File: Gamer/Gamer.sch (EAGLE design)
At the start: 44 parts, among them J1 HEADER-1X8, J2 HEADER-1X8, J3 HEADER-1X8, J4 HEADER-1X8, J5 HEADER-1X8, J6 HEADER-1X8, J7 HEADER-1X8, J8 HEADER-1X8, U1 MMA8653FCR1, U2 ATTINY48, U3 ULN2803AFWG, U4 ATTINY48, U5 ULN2803AFWG, U6 ATTINY48, U7 ULN2803AFWG, U8 ATTINY48, U9 ULN2803AFWG

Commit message: gamer - partial routing, with ground plane and vias, and some hand routing
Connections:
- net 3.3V_2 renamed 3V3_2
- removed net 3.3V_1: P1.1
- removed net GND: A.1, B.1, C1.2, C2.2, C3.2, C4.2, C5.2, C6.2, C7.2, C8.2, DOWN.4, LEFT.4, P1.9, PROG1.6, PROG2.6, PROG3.6, PROG4.6, RIGHT.4, SELECT.4, START.4, U1.AAGND, U1.AGND, U1.GND, U2.AGND, U2.GND, U3.GND, U4.AGND, U4.GND, U5.GND, U6.AGND, U6.GND, U7.GND, U8.AGND, U8.GND, U9.GND, UP.4
- removed net SCL: R1.1, U1.SCL
- removed net SDA: R2.1, U1.SDA
- removed net VCC: C1.1, C2.1, C4.1, C5.1, C6.1, C7.1, C8.1, PROG1.2, PROG2.2, PROG3.2, PROG4.2, R1.2, R2.2, R3.1, R4.1, R5.1, R6.1, U1.VDD, U1.VDDIO, U2.AVCC, U2.VCC, U3.COMMON, U4.AVCC, U4.VCC, U5.COMMON, U6.AVCC, U6.VCC, U7.COMMON, U8.AVCC, U8.VCC, U9.COMMON
- new net 3V3: C1.1, C2.1, C4.1, C5.1, C6.1, C7.1, C8.1, P1.1, PROG1.2, PROG2.2, PROG3.2, PROG4.2, R1.2, R2.2, R3.1, R4.1, R5.1, R6.1, U1.VDD, U1.VDDIO, U2.AVCC, U2.VCC, U3.COMMON, U4.AVCC, U4.VCC, U5.COMMON, U6.AVCC, U6.VCC, U7.COMMON, U8.AVCC, U8.VCC, U9.COMMON
- new net EEE: A.1, B.1, C1.2, C2.2, C3.2, C4.2, C5.2, C6.2, C7.2, C8.2, DOWN.4, LEFT.4, P1.9, PROG1.6, PROG2.6, PROG3.6, PROG4.6, RIGHT.4, SELECT.3, START.3, U1.AAGND, U1.AGND, U1.GND, U2.AGND, U2.GND, U3.GND, U4.AGND, U4.GND, U5.GND, U6.AGND, U6.GND, U7.GND, U8.AGND, U8.GND, U9.GND, UP.4
- new net N$1: START.4
- net 2/SDA: now also R2.1, U1.SDA
- net 3/SCL: now also R1.1, U1.SCL
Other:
- moved on the sheet: R2
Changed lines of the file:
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@@
 <part name="SUPPLY20" library="SparkFun-Aesthetics" deviceset="VCC" device=""/>
 <part name="GND23" library="SparkFun-Aesthetics" deviceset="GND" device=""/>
-<part name="R1" library="AccelBreakout" deviceset="R-US_" device="R0603" value="10K"/>
 <part name="R2" library="AccelBreakout" deviceset="R-US_" device="R0603" value="10K"/>
 <part name="P1" library="HeaderConnectorBoard" deviceset="PINHD-2X20" device=""/>
@@
 <part name="J7" library="LED_Matrix" deviceset="HEADER-1X8" device=""/>
 <part name="J8" library="LED_Matrix" deviceset="HEADER-1X8" device=""/>
+<part name="SUPPLY29" library="SparkFun-Aesthetics" deviceset="VCC" device=""/>
+<part name="GND30" library="SparkFun-Aesthetics" deviceset="GND" device=""/>
+<part name="R1" library="AccelBreakout" deviceset="R-US_" device="R0603" value="10K"/>
 </parts>
 <sheets>
@@
 <instance part="GND21" gate="1" x="172.72" y="45.72"/>
 <instance part="GND22" gate="1" x="137.16" y="20.32"/>
-<instance part="GND38" gate="1" x="60.96" y="142.24"/>
-<instance part="GND39" gate="1" x="60.96" y="111.76"/>
+<instance part="GND38" gate="1" x="22.86" y="142.24"/>
+<instance part="GND39" gate="1" x="22.86" y="111.76"/>
 <instance part="FRAME1" gate="G$1" x="0" y="0"/>
 <instance part="FRAME1" gate="G$2" x="147.32" y="0"/>
@@
 <instance part="C4" gate="G$1" x="228.6" y="99.06"/>
 <instance part="SUPPLY18" gate="G$1" x="154.94" y="121.92"/>
-<instance part="SUPPLY19" gate="G$1" x="218.44" y="127"/>
+<instance part="SUPPLY19" gate="G$1" x="218.44" y="134.62"/>
 <instance part="SUPPLY20" gate="G$1" x="236.22" y="106.68"/>
 <instance part="GND23" gate="1" x="220.98" y="86.36"/>
-<instance part="R1" gate="G$1" x="154.94" y="116.84" rot="R90"/>
-<instance part="R2" gate="G$1" x="218.44" y="121.92" rot="R90"/>
+<instance part="R2" gate="G$1" x="218.44" y="127" rot="R90"/>
 <instance part="P1" gate="A" x="109.22" y="134.62"/>
 <instance part="START" gate="G$1" x="40.64" y="152.4"/>
 <instance part="SELECT" gate="G$1" x="40.64" y="121.92"/>
+<instance part="SUPPLY29" gate="G$1" x="99.06" y="165.1"/>
+<instance part="GND30" gate="1" x="83.82" y="142.24"/>
+<instance part="R1" gate="G$1" x="154.94" y="116.84" rot="R90"/>
 </instances>
 <busses>
 </busses>
 <nets>
-<net name="GND" class="0">
+<net name="EEE" class="0">
 <segment>
 <pinref part="RIGHT" gate="G$1" pin="4"/>
@@
 </segment>
 <segment>
-<wire x1="60.96" y1="147.32" x2="60.96" y2="144.78" width="0.1524" layer="91"/>
+<pinref part="START" gate="G$1" pin="3"/>
+<wire x1="22.86" y1="147.32" x2="27.94" y2="147.32" width="0.1524" layer="91"/>
 <pinref part="GND38" gate="1" pin="GND"/>
-<pinref part="START" gate="G$1" pin="4"/>
-<wire x1="60.96" y1="147.32" x2="53.34" y2="147.32" width="0.1524" layer="91"/>
-</segment>
-<segment>
-<wire x1="60.96" y1="116.84" x2="60.96" y2="114.3" width="0.1524" layer="91"/>
+<wire x1="22.86" y1="144.78" x2="22.86" y2="147.32" width="0.1524" layer="91"/>
+</segment>
+<segment>
 <pinref part="GND39" gate="1" pin="GND"/>
-<wire x1="60.96" y1="116.84" x2="53.34" y2="116.84" width="0.1524" layer="91"/>
-<pinref part="SELECT" gate="G$1" pin="4"/>
+<pinref part="SELECT" gate="G$1" pin="3"/>
+<wire x1="22.86" y1="114.3" x2="22.86" y2="116.84" width="0.1524" layer="91"/>
+<wire x1="22.86" y1="116.84" x2="27.94" y2="116.84" width="0.1524" layer="91"/>
 </segment>
 <segment>
@@
 </segment>
 <segment>
-<label x="96.52" y="147.32" size="1.016" layer="95" rot="R180" xref="yes"/>
-<wire x1="106.68" y1="147.32" x2="96.52" y2="147.32" width="0.1524" layer="91"/>
+<label x="78.74" y="147.32" size="1.016" layer="95" rot="R180" xref="yes"/>
+<wire x1="106.68" y1="147.32" x2="83.82" y2="147.32" width="0.1524" layer="91"/>
 <pinref part="P1" gate="A" pin="9"/>
-</segment>
-</net>
-<net name="VCC" class="0">
+<pinref part="GND30" gate="1" pin="GND"/>
+<wire x1="83.82" y1="147.32" x2="78.74" y2="147.32" width="0.1524" layer="91"/>
+<wire x1="83.82" y1="144.78" x2="83.82" y2="147.32" width="0.1524" layer="91"/>
+<junction x="83.82" y="147.32"/>
+</segment>
+</net>
+<net name="3V3" class="0">
 <segment>
 <pinref part="SUPPLY17" gate="G$1" pin="VCC"/>
@@
 <pinref part="SUPPLY19" gate="G$1" pin="VCC"/>
 <pinref part="R2" gate="G$1" pin="2"/>
+<wire x1="218.44" y1="134.62" x2="218.44" y2="132.08" width="0.1524" layer="91"/>
+</segment>
+<segment>
+<label x="96.52" y="157.48" size="1.016" layer="95" rot="R180" xref="yes"/>
+<wire x1="106.68" y1="157.48" x2="99.06" y2="157.48" width="0.1524" layer="91"/>
+<pinref part="P1" gate="A" pin="1"/>
+<wire x1="99.06" y1="157.48" x2="96.52" y2="157.48" width="0.1524" layer="91"/>
+<wire x1="99.06" y1="157.48" x2="99.06" y2="165.1" width="0.1524" layer="91"/>
+<junction x="99.06" y="157.48"/>
+<pinref part="SUPPLY29" gate="G$1" pin="VCC"/>
 </segment>
 </net>
@@
 <pinref part="U1" gate="G$1" pin="BYP"/>
 <wire x1="170.18" y1="101.6" x2="187.96" y2="101.6" width="0.1524" layer="91"/>
-</segment>
-</net>
-<net name="SDA" class="0">
-<segment>
-<pinref part="U1" gate="G$1" pin="SDA"/>
-<wire x1="218.44" y1="116.84" x2="223.52" y2="116.84" width="0.1524" layer="91"/>
-<label x="223.52" y="116.84" size="1.778" layer="95" xref="yes"/>
-<pinref part="R2" gate="G$1" pin="1"/>
-<junction x="218.44" y="116.84"/>
-</segment>
-</net>
-<net name="SCL" class="0">
-<segment>
-<pinref part="U1" gate="G$1" pin="SCL"/>
-<wire x1="187.96" y1="111.76" x2="154.94" y2="111.76" width="0.1524" layer="91"/>
-<label x="154.94" y="111.76" size="1.778" layer="95" rot="R180" xref="yes"/>
-<pinref part="R1" gate="G$1" pin="1"/>
-<junction x="154.94" y="111.76"/>
 </segment>
 </net>
@@
 </segment>
 </net>
-<net name="3.3V_1" class="0">
-<segment>
-<label x="96.52" y="157.48" size="1.016" layer="95" rot="R180" xref="yes"/>
-<wire x1="106.68" y1="157.48" x2="96.52" y2="157.48" width="0.1524" layer="91"/>
-<pinref part="P1" gate="A" pin="1"/>
-</segment>
-</net>
 <net name="2/SDA" class="0">
 <segment>
@@
 <pinref part="P1" gate="A" pin="3"/>
 </segment>
+<segment>
+<pinref part="U1" gate="G$1" pin="SDA"/>
+<label x="223.52" y="116.84" size="1.778" layer="95" xref="yes"/>
+<pinref part="R2" gate="G$1" pin="1"/>
+<wire x1="218.44" y1="121.92" x2="218.44" y2="116.84" width="0.1524" layer="91"/>
+<wire x1="223.52" y1="116.84" x2="218.44" y2="116.84" width="0.1524" layer="91"/>
+<junction x="218.44" y="116.84"/>
+</segment>
 </net>
 <net name="3/SCL" class="0">
@@
 <pinref part="P1" gate="A" pin="5"/>
 </segment>
+<segment>
+<pinref part="U1" gate="G$1" pin="SCL"/>
+<label x="149.86" y="111.76" size="1.778" layer="95" rot="R180" xref="yes"/>
+<wire x1="154.94" y1="111.76" x2="149.86" y2="111.76" width="0.1524" layer="91"/>
+<pinref part="R1" gate="G$1" pin="1"/>
+<junction x="154.94" y="111.76"/>
+<wire x1="154.94" y1="111.76" x2="187.96" y2="111.76" width="0.1524" layer="91"/>
+</segment>
 </net>
 <net name="4" class="0">
@@
 </segment>
 </net>
-<net name="3.3V_2" class="0">
+<net name="3V3_2" class="0">
 <segment>
 <label x="96.52" y="137.16" size="1.016" layer="95" rot="R180" xref="yes"/>
@@
 <wire x1="114.3" y1="124.46" x2="124.46" y2="124.46" width="0.1524" layer="91"/>
 <label x="124.46" y="124.46" size="1.016" layer="95" xref="yes"/>
+</segment>
+</net>
+<net name="N$1" class="0">
+<segment>
+<pinref part="START" gate="G$1" pin="4"/>
+<wire x1="60.96" y1="147.32" x2="53.34" y2="147.32" width="0.1524" layer="91"/>
 </segment>
 </net>
@@
 </segment>
 </net>
-<net name="VCC" class="0">
+<net name="3V3" class="0">
 <segment>
 <pinref part="SUPPLY1" gate="G$1" pin="VCC"/>
@@
 </segment>
 </net>
-<net name="GND" class="0">
+<net name="EEE" class="0">
 <segment>
 <pinref part="U2" gate="G$1" pin="GND"/>
@@
 </segment>
 </net>
-<net name="VCC" class="0">
+<net name="3V3" class="0">
 <segment>
 <pinref part="SUPPLY6" gate="G$1" pin="VCC"/>
@@
 </segment>
 </net>
-<net name="GND" class="0">
+<net name="EEE" class="0">
 <segment>
 <pinref part="U4" gate="G$1" pin="GND"/>
@@
 </segment>
 </net>
-<net name="VCC" class="0">
+<net name="3V3" class="0">
 <segment>
 <pinref part="SUPPLY13" gate="G$1" pin="VCC"/>
@@
 </segment>
 </net>
-<net name="GND" class="0">
+<net name="EEE" class="0">
 <segment>
 <pinref part="U6" gate="G$1" pin="GND"/>
@@
 </segment>
 </net>
-<net name="VCC" class="0">
+<net name="3V3" class="0">
 <segment>
 <pinref part="SUPPLY23" gate="G$1" pin="VCC"/>
@@
 </segment>
 </net>
-<net name="GND" class="0">
+<net name="EEE" class="0">
 <segment>
 <pinref part="U8" gate="G$1" pin="GND"/>

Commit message: gamer - more manual routing
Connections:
- net EEE renamed GND
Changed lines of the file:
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@@
 </busses>
 <nets>
-<net name="EEE" class="0">
+<net name="GND" class="0">
 <segment>
 <pinref part="RIGHT" gate="G$1" pin="4"/>
@@
 </segment>
 </net>
-<net name="EEE" class="0">
+<net name="GND" class="0">
 <segment>
 <pinref part="U2" gate="G$1" pin="GND"/>
@@
 </segment>
 </net>
-<net name="EEE" class="0">
+<net name="GND" class="0">
 <segment>
 <pinref part="U4" gate="G$1" pin="GND"/>
@@
 </segment>
 </net>
-<net name="EEE" class="0">
+<net name="GND" class="0">
 <segment>
 <pinref part="U6" gate="G$1" pin="GND"/>
@@
 </segment>
 </net>
-<net name="EEE" class="0">
+<net name="GND" class="0">
 <segment>
 <pinref part="U8" gate="G$1" pin="GND"/>

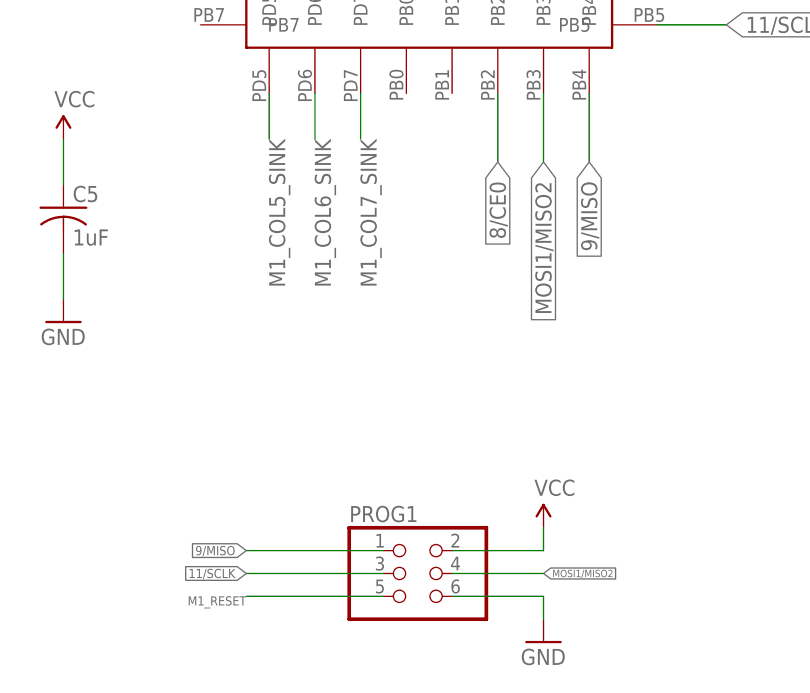
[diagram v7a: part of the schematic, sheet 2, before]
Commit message: gamer - Order of SPI chain was backwards
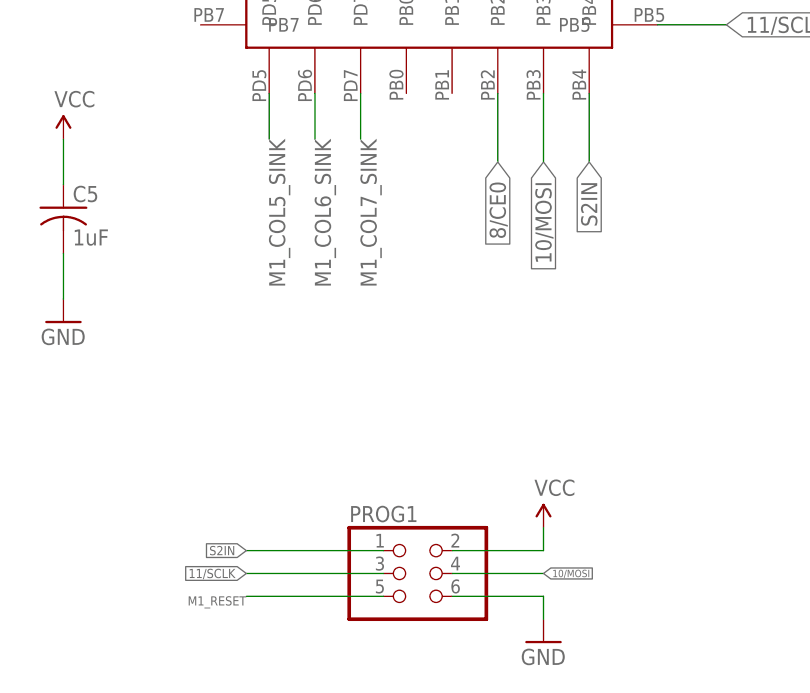
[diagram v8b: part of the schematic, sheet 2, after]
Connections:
- removed net 10/MISO: PROG4.4, U8.PB3
- removed net MOSI1/MISO2: PROG1.4, PROG2.1, U2.PB3, U4.PB4
- removed net MOSI2/MISO3: PROG2.4, PROG3.1, U4.PB3, U6.PB4
- removed net MOSI3/MISO4: PROG3.4, PROG4.1, U6.PB3, U8.PB4
- new net S2IN: PROG1.1, PROG2.4, U2.PB4, U4.PB3
- new net S3IN: PROG2.1, PROG3.4, U4.PB4, U6.PB3
- new net S4IN: PROG3.1, PROG4.4, U6.PB4, U8.PB3
- net 10/MOSI: now also PROG1.4, U2.PB3
- net 9/MISO: now also PROG4.1, U8.PB4; no longer PROG1.1, U2.PB4
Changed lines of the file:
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@@
 </segment>
 </net>
-<net name="9/MISO" class="0">
+<net name="S2IN" class="0">
 <segment>
 <pinref part="U2" gate="G$1" pin="PB4"/>
@@
 </segment>
 </net>
-<net name="MOSI1/MISO2" class="0">
+<net name="10/MOSI" class="0">
 <segment>
 <pinref part="U2" gate="G$1" pin="PB3"/>
@@
 </segment>
 </net>
-<net name="MOSI1/MISO2" class="0">
+<net name="S3IN" class="0">
 <segment>
 <pinref part="U4" gate="G$1" pin="PB4"/>
@@
 </segment>
 </net>
-<net name="MOSI2/MISO3" class="0">
+<net name="S2IN" class="0">
 <segment>
 <pinref part="U4" gate="G$1" pin="PB3"/>
@@
 </segment>
 </net>
-<net name="MOSI2/MISO3" class="0">
+<net name="S4IN" class="0">
 <segment>
 <pinref part="U6" gate="G$1" pin="PB4"/>
@@
 </segment>
 </net>
-<net name="MOSI3/MISO4" class="0">
+<net name="S3IN" class="0">
 <segment>
 <pinref part="U6" gate="G$1" pin="PB3"/>
@@
 </segment>
 </net>
-<net name="MOSI3/MISO4" class="0">
+<net name="9/MISO" class="0">
 <segment>
 <pinref part="U8" gate="G$1" pin="PB4"/>
@@
 </segment>
 </net>
-<net name="10/MISO" class="0">
+<net name="S4IN" class="0">
 <segment>
 <pinref part="U8" gate="G$1" pin="PB3"/>
